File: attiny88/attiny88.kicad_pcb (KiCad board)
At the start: 2 copper layers, 100 x 40 mm, 43 parts, among them IC1 ATTINY88-A, P1 CONN_01X04, P2 CONN_02X03, P3 CONN_01X04, P4 CONN_01X04

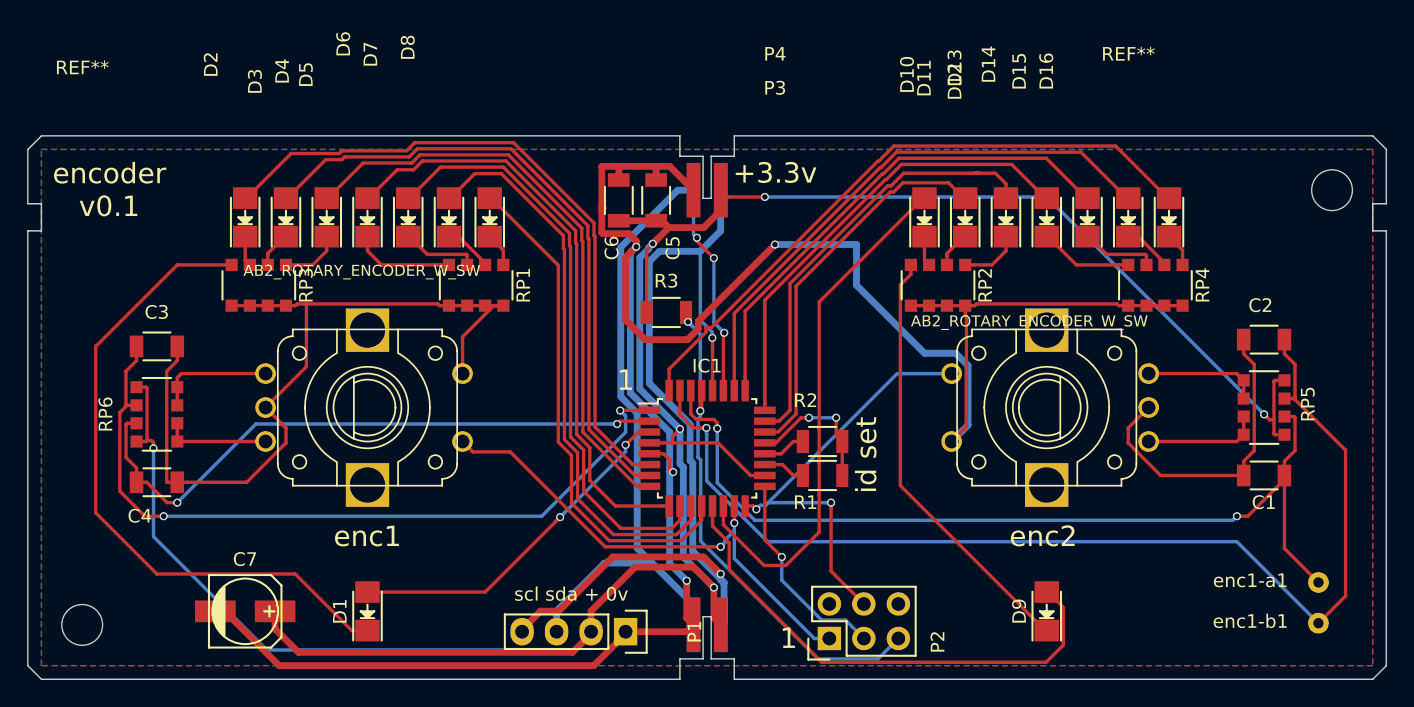
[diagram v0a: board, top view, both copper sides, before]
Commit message: rev conn diode, smaller caps, cleaner layout, wider slots
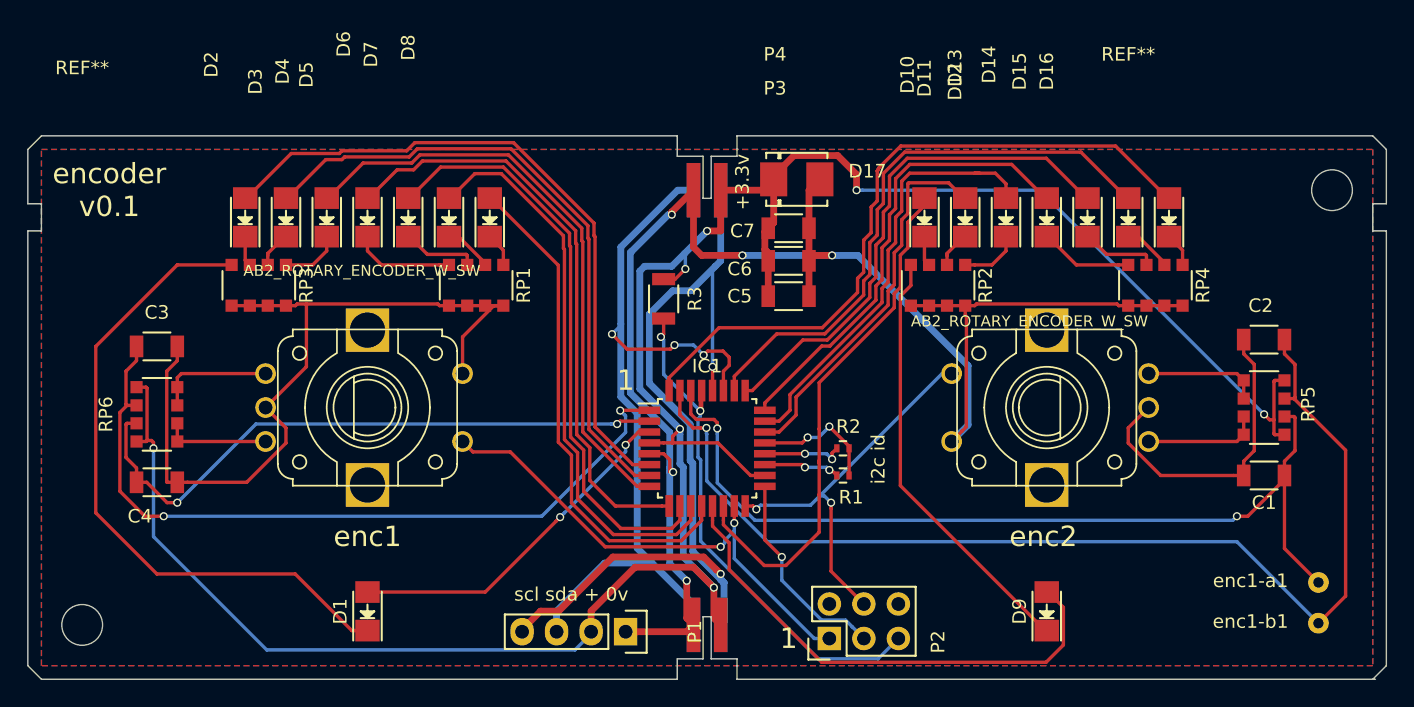
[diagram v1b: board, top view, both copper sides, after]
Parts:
- added D17: 1A, Diodes_SMD:DO-214BA, F.Cu at (171.6, 53.2)
- C5: value C -> 1u
- C6: value C -> 0.1u
- C7: value C -> 10u; footprint Capacitors_SMD:c_elec_5x5.3 -> Capacitors_SMD:C_1206
- R1, R2: footprint Resistors_SMD:R_1206 -> Resistors_SMD:R_0402
- moved C7 48.9 mm to (171.0, 56.8)
- moved C6 13.3 mm to (171.0, 59.2), turned to 0 degrees
- moved C5 12.0 mm to (171.0, 61.8), turned to 0 degrees
- moved R2 1.58 mm to (175.0, 73.0)
- moved R1 1.50 mm to (175.0, 75.0)
- moved R3 1.02 mm to (161.8, 62.0), turned to 270 degrees
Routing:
- net Earth: track 258.5 -> 211.8 mm, vias 6 -> 7
- net +3V3: track 199.2 -> 179.5 mm, vias 6 -> 7
- net led15: track 46.9 -> 50.9 mm
- net enc1-s: track 32.8 -> 28.9 mm
- net id1: track 3.17 -> 6.06 mm, vias 0 -> 2
- net id0: track 3.13 -> 5.63 mm, vias 0 -> 2
- net scl: track 67.2 -> 64.8 mm
- net sda: track 62.8 -> 60.6 mm
- net led14: track 41.0 -> 42.7 mm
- net led13: track 36.9 -> 37.9 mm
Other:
- outline, holes or cut-outs redrawn
- board text added: "i2c id"
- board text removed: "id set"

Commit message: fixed miso/mosi mixup
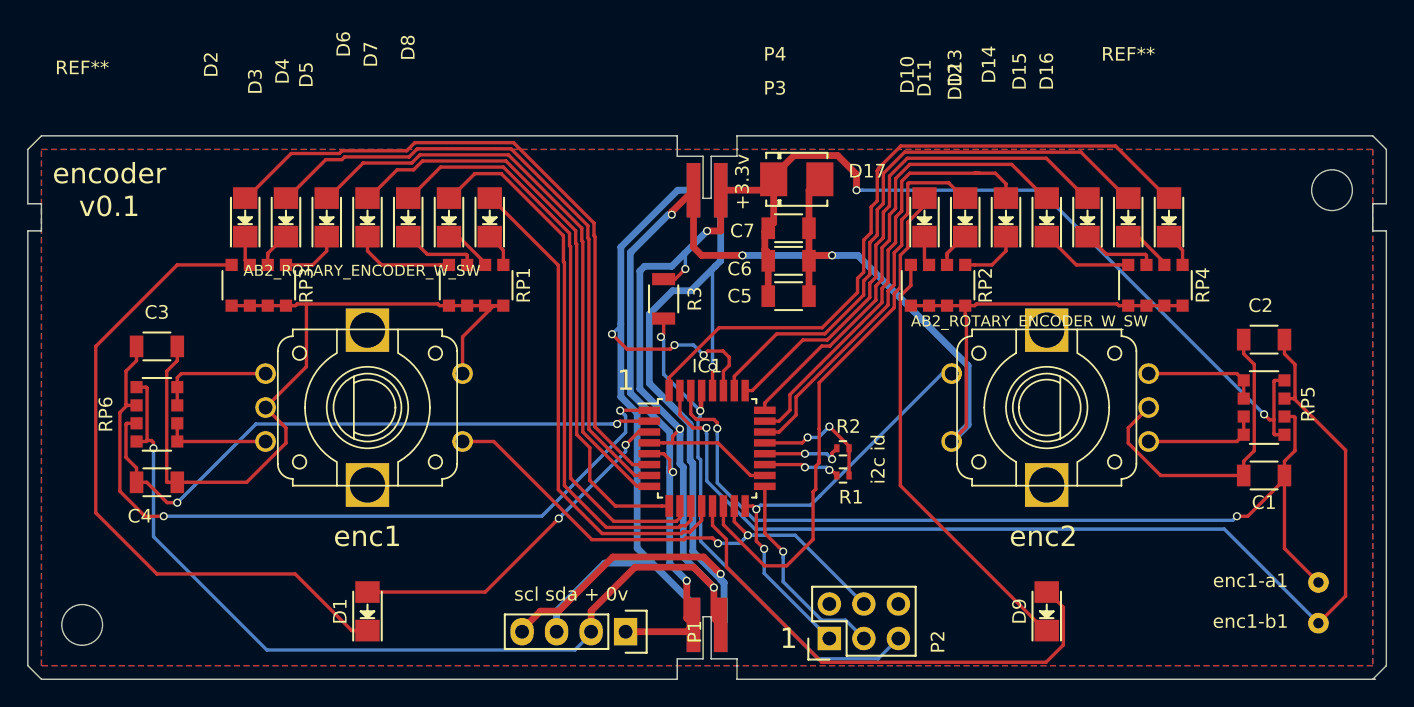
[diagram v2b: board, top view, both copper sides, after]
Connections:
- IC1 pad 15: miso -> enc2-s
- IC1 pad 16: enc1-s -> miso
- P2 pad 4: enc1-s -> enc2-s
- ROT_ENC1 pad 4: miso -> enc2-s
- ROT_ENC2 pad 4: enc1-s -> miso
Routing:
- net enc2-s: track 0.00 -> 37.7 mm, vias 0 -> 2
- net enc1-s: track 28.9 -> 0.00 mm, vias 2 -> 0
- net miso: track 37.1 -> 31.2 mm
- net led5: track 43.8 -> 43.2 mm

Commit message: sent to fab
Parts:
- removed P4: CONN_01X04, fp:avx
- removed R1, R2: R, Resistors_SMD:R_0402
- added Q1: MMBF170, TO_SOT_Packages_SMD:SOT-323, F.Cu at (150.1, 81.6)
- added gpio: testpoint, fp:testpoint, F.Cu at (152.4, 70.1)
- added pwm: gpio, fp:testpoint, F.Cu at (154.1, 79.2)
- P1: footprint Pin_Headers:Pin_Header_Straight_1x04 -> Pin_Headers:Pin_Header_Angled_1x04
- P3: footprint fp:avx -> fp:molex 4way cgrid
- moved D17 37.1 mm to (155.3, 86.5)
- moved P1 32.6 mm to (161.2, 54.0), turned to 90 degrees
- moved C5 26.7 mm to (155.4, 83.5)
- moved P3 26.5 mm to (161.2, 80.2)
- moved R3 15.2 mm to (176.4, 66.2)
- moved C7 8.74 mm to (162.3, 57.6), turned to 180 degrees
- moved C6 6.12 mm to (165.0, 60.4), turned to 180 degrees
- moved IC1 3.50 mm to (165.0, 69.5), turned to 270 degrees
- moved P2 0.99 mm to (174.9, 86.5)
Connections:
- IC1 pad 13: led8 -> pwm
- IC1 pad 14: led9 -> gpio1
- IC1 pad 19: id0 -> led8
- IC1 pad 20: id1 -> led9
- RP1 pad 5: Earth -> Net-(Q1-Pad3)
- RP1 pad 6: Earth -> Net-(Q1-Pad3)
- RP1 pad 7: Earth -> Net-(Q1-Pad3)
- RP1 pad 8: Earth -> Net-(Q1-Pad3)
- RP2 pad 5: Earth -> Net-(Q1-Pad3)
- RP2 pad 6: Earth -> Net-(Q1-Pad3)
- RP2 pad 7: Earth -> Net-(Q1-Pad3)
- RP2 pad 8: Earth -> Net-(Q1-Pad3)
- RP3 pad 5: Earth -> Net-(Q1-Pad3)
- RP3 pad 6: Earth -> Net-(Q1-Pad3)
- RP3 pad 7: Earth -> Net-(Q1-Pad3)
- RP3 pad 8: Earth -> Net-(Q1-Pad3)
- RP4 pad 5: Earth -> Net-(Q1-Pad3)
- RP4 pad 6: Earth -> Net-(Q1-Pad3)
- RP4 pad 7: Earth -> Net-(Q1-Pad3)
- RP4 pad 8: Earth -> Net-(Q1-Pad3)
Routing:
- net Net-(Q1-Pad3): track 0.00 -> 136.3 mm
- net Earth: track 211.8 -> 120.2 mm, vias 7 -> 1
- net scl: track 64.8 -> 39.5 mm
- net sda: track 60.6 -> 38.0 mm, vias 3 -> 2
- net pwm: track 0.00 -> 21.5 mm, vias 0 -> 2
- net miso: track 31.2 -> 51.8 mm, vias 2 -> 0
- net led6: track 41.3 -> 24.8 mm
- net led7: track 37.0 -> 21.3 mm
- net led5: track 43.2 -> 27.8 mm
- net +3V3: track 179.5 -> 193.8 mm, vias 7 -> 3
- net led4: track 44.0 -> 30.1 mm
- net enc1-b: track 81.7 -> 68.5 mm, vias 1 -> 2
- net sck: track 15.3 -> 27.8 mm, vias 1 -> 0
- net reset: track 39.5 -> 28.3 mm
- net enc2-b: track 46.2 -> 57.4 mm
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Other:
- outline, holes or cut-outs redrawn
- board text added: "0v 3.3v sda scl"
- board text added: "ven.nz/modbox"
- board text removed: "+3.3v"
- board text removed: "i2c id"
- board text removed: "scl sda + 0v"
